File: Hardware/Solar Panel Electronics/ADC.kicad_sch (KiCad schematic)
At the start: 19 parts, among them U8 ADS131M04

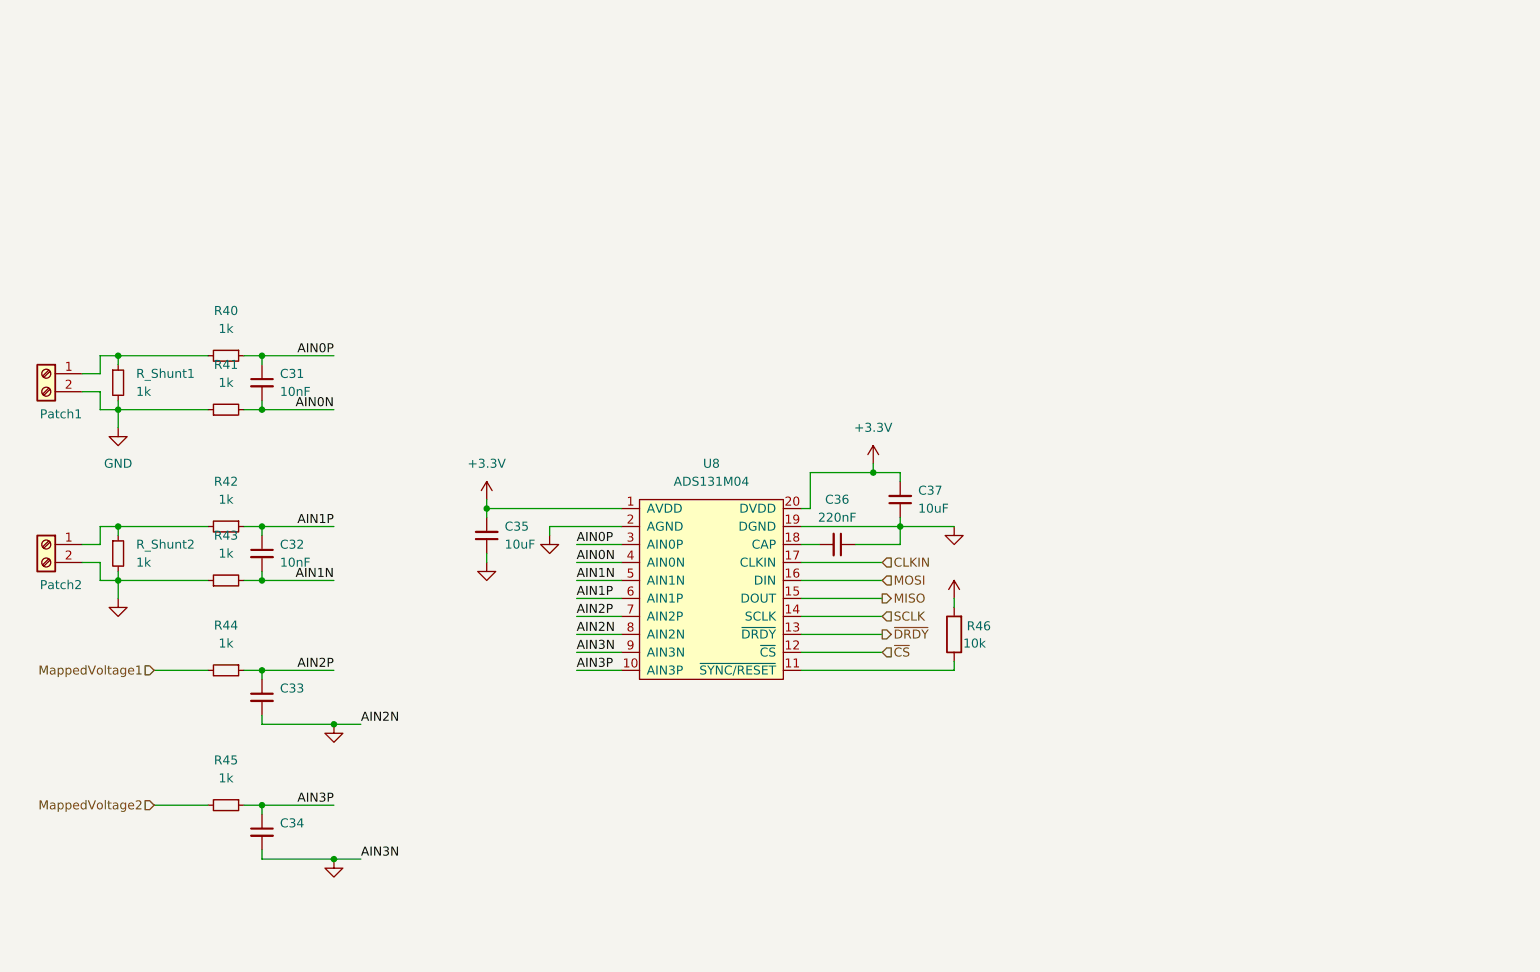
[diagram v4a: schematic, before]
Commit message: Added another ADS component. Layout and routing can be continued.
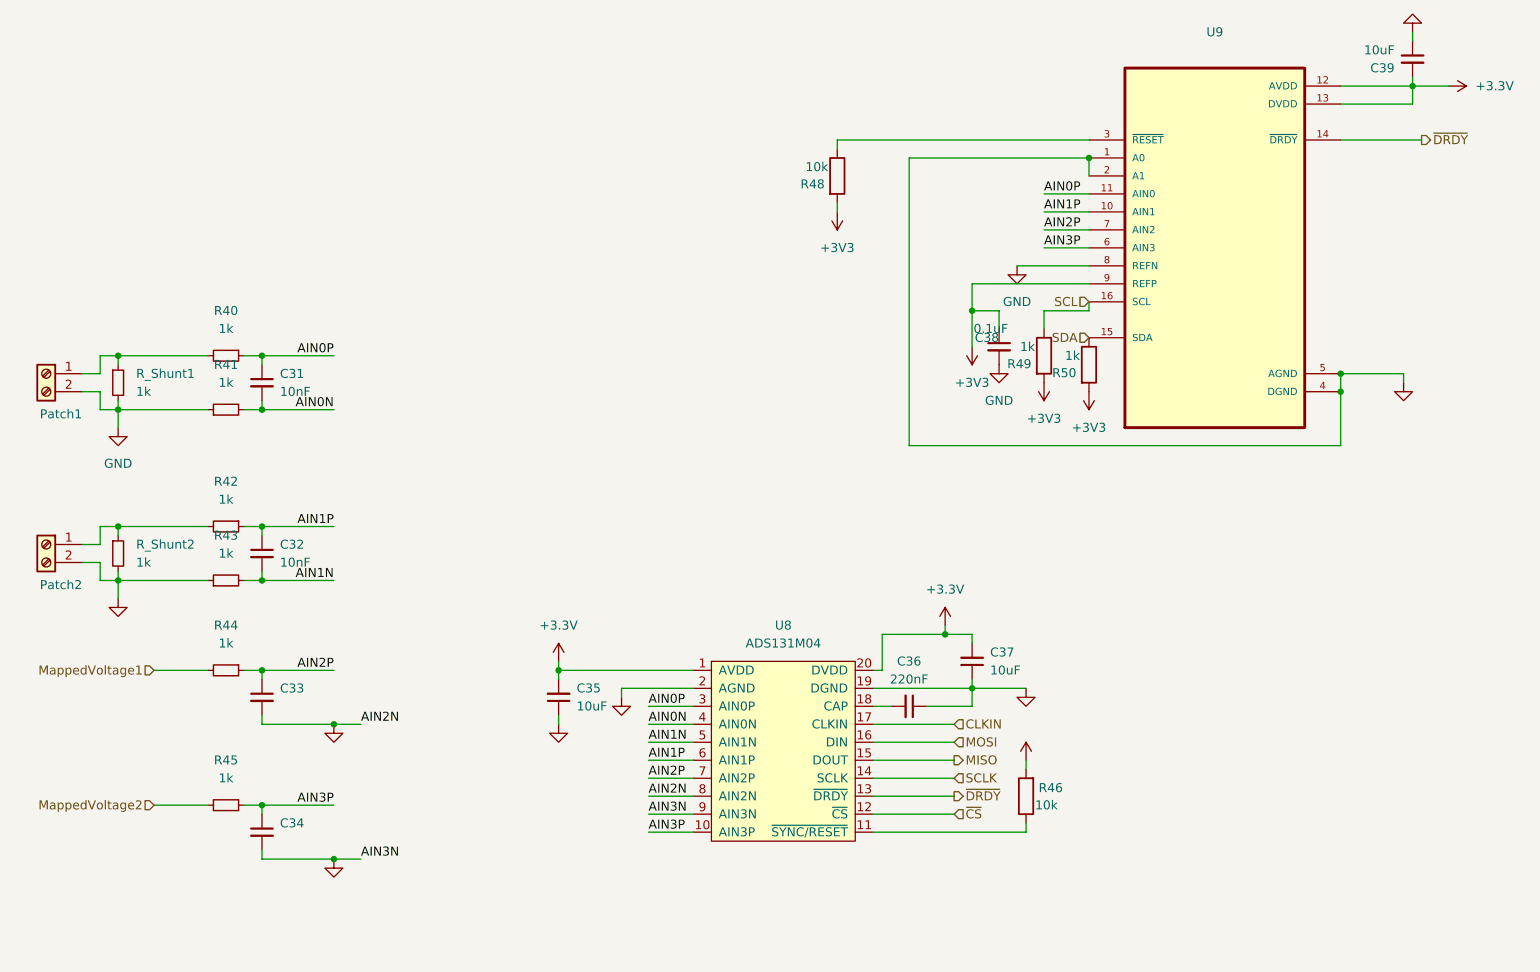
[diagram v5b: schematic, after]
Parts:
- added C38: 0.1uF, Capacitor_SMD:C_0603_1608Metric, symbol Device:C_Small
- added C39: 10uF, Capacitor_SMD:C_0603_1608Metric, symbol Device:C_Small
- added R48: 10k, Resistor_SMD:R_0603_1608Metric, symbol Device:R
- added R49, R50: 1k, Resistor_SMD:R_0603_1608Metric, symbol Device:R
- added U9: (no value), symbol ADS1219IPWT:ADS1219IPWT
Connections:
- net +3V3: now also C38.1, C39.2, R48.2, R49.2, R50.2, U9.12 (AVDD), U9.13 (DVDD), U9.9 (REFP)
- net AIN0P: now also U9.11 (AIN0)
- net AIN1P: now also U9.10 (AIN1)
- net AIN2P: now also U9.7 (AIN2)
- net AIN3P: now also U9.6 (AIN3)
- net GND: now also C38.2, C39.1, U9.1 (A0), U9.2 (A1), U9.4 (DGND), U9.5 (AGND), U9.8 (REFN)
- net ~{DRDY}: now also U9.14 (~{DRDY})
- new net: R48.1, U9.3 (~{RESET})
- new net SCL: R49.1, U9.16 (SCL)
- new net SDA: R50.1, U9.15 (SDA)
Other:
- moved on the sheet: C35, C36, C37, R46, U8

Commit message: ICARUS v2
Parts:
- removed C35, C37: 10uF, Capacitor_SMD:C_0603_1608Metric, symbol Device:C_Small
- removed C36: 220nF, Capacitor_SMD:C_0603_1608Metric, symbol Device:C_Small
- removed R46: 10k, Resistor_SMD:R_0603_1608Metric, symbol Device:R
- removed U8: ADS131M04, Package_DFN_QFN:WQFN-20-1EP_3x3mm_P0.4mm_EP1.7x1.7mm_ThermalVias, symbol iclr:ADS131M04
- U9: value (none) -> ADS1219IPWT; footprint (none) -> ADS1219IPWT:SOP65P640X120-16N
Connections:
- net GND: no longer C33.2, C34.2, Patch1.2 (Pin_2), Patch2.2 (Pin_2), R41.1, R43.1, R_Shunt1.2, R_Shunt2.2, U9.5 (AGND), U9.8 (REFN)
- new net GNDA: C33.2, C34.2, Patch1.2 (Pin_2), Patch2.2 (Pin_2), R41.1, R43.1, R_Shunt1.2, R_Shunt2.2, U9.5 (AGND), U9.8 (REFN)

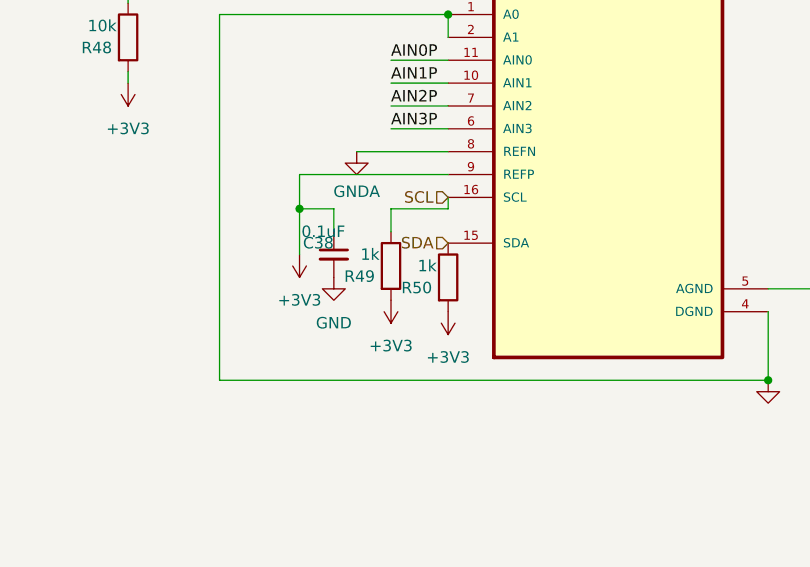
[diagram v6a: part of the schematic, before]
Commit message: attempt to fix vreg and charger
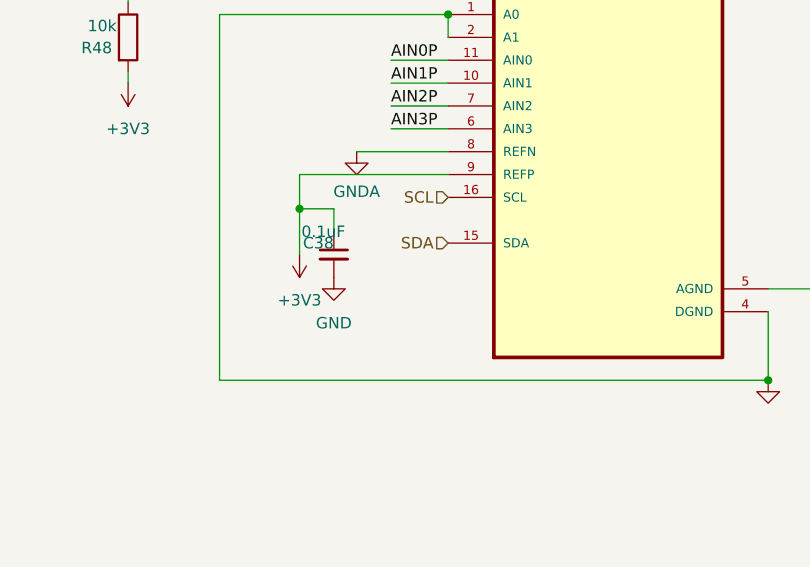
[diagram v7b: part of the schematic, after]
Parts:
- removed R49, R50: 1k, Resistor_SMD:R_0603_1608Metric, symbol Device:R
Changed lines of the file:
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@@
-    (stroke (width 0) (type default) (color 0 0 0 0))
-  )
-  (wire (pts (xy 228.6 57.15) (xy 222.25 57.15))
     (stroke (width 0) (type default) (color 0 0 0 0))
   )
@@
     (stroke (width 0) (type default) (color 0 0 0 0))
   )
-  (wire (pts (xy 228.6 55.88) (xy 228.6 57.15))
-    (stroke (width 0) (type default) (color 0 0 0 0))
-  )
   (wire (pts (xy 212.09 57.15) (xy 212.09 62.23))
     (stroke (width 0) (type default) (color 0 0 0 0))
@@
   )
   (wire (pts (xy 88.9 92.71) (xy 88.9 95.25))
-    (stroke (width 0) (type default) (color 0 0 0 0))
-  )
-  (wire (pts (xy 222.25 57.15) (xy 222.25 59.69))
     (stroke (width 0) (type default) (color 0 0 0 0))
   )
@@
     (pin "1")
   )
-  (symbol (lib_id "power:+3V3") (at 222.25 67.31 180) (unit 1)
-    (in_bom yes) (on_board yes) (fields_autoplaced)
-    (property "Reference" "#PWR038" (id 0) (at 222.25 63.5 0)
-      (effects (font (size 1.27 1.27)) hide)
-    )
-    (property "Value" "+3V3" (id 1) (at 222.25 72.39 0))
-    (property "Footprint" "" (id 2) (at 222.25 67.31 0)
-      (effects (font (size 1.27 1.27)) hide)
-    )
-    (property "Datasheet" "" (id 3) (at 222.25 67.31 0)
-      (effects (font (size 1.27 1.27)) hide)
-    )
-    (pin "1")
-  )
   (symbol (lib_id "power:GNDA") (at 91.44 73.66 0) (unit 1)
     (in_bom yes) (on_board yes) (fields_autoplaced)
@@
     )
     (property "Datasheet" "" (id 3) (at 91.44 73.66 0)
-      (effects (font (size 1.27 1.27)) hide)
-    )
-    (pin "1")
-  )
-  (symbol (lib_id "power:+3V3") (at 228.6 68.58 180) (unit 1)
-    (in_bom yes) (on_board yes) (fields_autoplaced)
-    (property "Reference" "#PWR039" (id 0) (at 228.6 64.77 0)
-      (effects (font (size 1.27 1.27)) hide)
-    )
-    (property "Value" "+3V3" (id 1) (at 228.6 73.66 0))
-    (property "Footprint" "" (id 2) (at 228.6 68.58 0)
-      (effects (font (size 1.27 1.27)) hide)
-    )
-    (property "Datasheet" "" (id 3) (at 228.6 68.58 0)
       (effects (font (size 1.27 1.27)) hide)
     )
@@
     )
     (property "Datasheet" "~" (id 3) (at 91.44 91.44 0)
-      (effects (font (size 1.27 1.27)) hide)
-    )
-    (pin "1")
-    (pin "2")
-  )
-  (symbol (lib_id "Device:R") (at 228.6 64.77 0) (unit 1)
-    (in_bom yes) (on_board yes)
-    (property "Reference" "R50" (id 0) (at 226.822 65.9384 0)
-      (effects (font (size 1.27 1.27)) (justify right))
-    )
-    (property "Value" "1k" (id 1) (at 227.33 63.5 0)
-      (effects (font (size 1.27 1.27)) (justify right))
-    )
-    (property "Footprint" "Resistor_SMD:R_0603_1608Metric" (id 2) (at 226.822 64.77 90)
-      (effects (font (size 1.27 1.27)) hide)
-    )
-    (property "Datasheet" "~" (id 3) (at 228.6 64.77 0)
       (effects (font (size 1.27 1.27)) hide)
     )
@@
       (effects (font (size 1.27 1.27)) hide)
     )
-    (pin "1")
-    (pin "2")
-  )
-  (symbol (lib_id "Device:R") (at 222.25 63.5 0) (unit 1)
-    (in_bom yes) (on_board yes)
-    (property "Reference" "R49" (id 0) (at 220.472 64.6684 0)
-      (effects (font (size 1.27 1.27)) (justify right))
-    )
-    (property "Value" "1k" (id 1) (at 220.98 62.23 0)
-      (effects (font (size 1.27 1.27)) (justify right))
-    )
-    (property "Footprint" "Resistor_SMD:R_0603_1608Metric" (id 2) (at 220.472 63.5 90)
-      (effects (font (size 1.27 1.27)) hide)
-    )
-    (property "Datasheet" "~" (id 3) (at 222.25 63.5 0)
-      (effects (font (size 1.27 1.27)) hide)
-    )
